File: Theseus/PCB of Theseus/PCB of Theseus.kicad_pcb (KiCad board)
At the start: 4 copper layers, 70 x 40 mm, 85 parts, among them J1 Conn_01x06_Socket, J2 Conn_01x06_Socket, J3 G125-MH104M4-04AD000P, J5 CN4 STDC14 (Programmer), J6 Micro SD Holder 0472192001, J7 4DB-P108-02, J8 Conn_01x12_Socket, Q1 DMG1012UW-7, Q2 DMG1012UW-7, U1 TPS565201DDC, U13 MAX6675, U2 MCP2562, U5 MX25L25645G, U6 STM32H750VBTx, Y1 ASE-4.000MHz-L-C-T

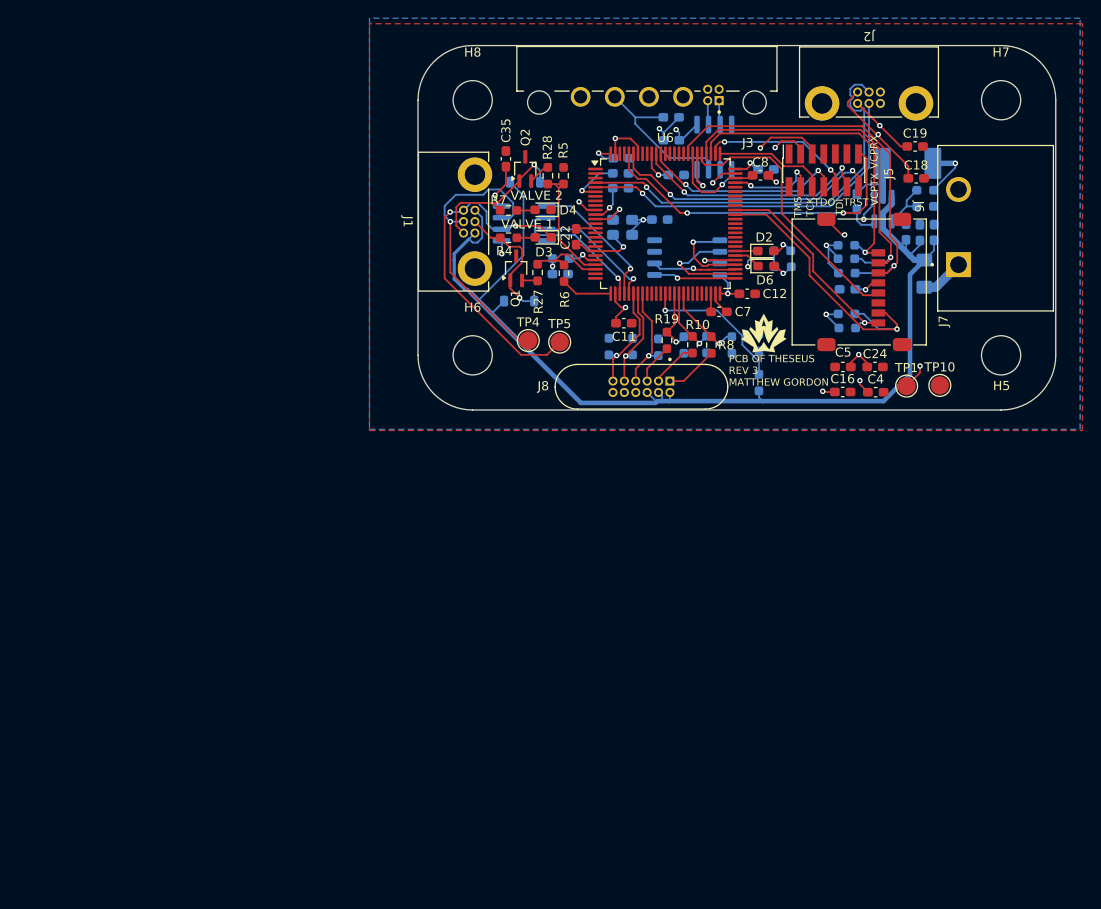
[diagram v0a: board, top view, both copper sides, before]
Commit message: layout and routing + minor schematic changes
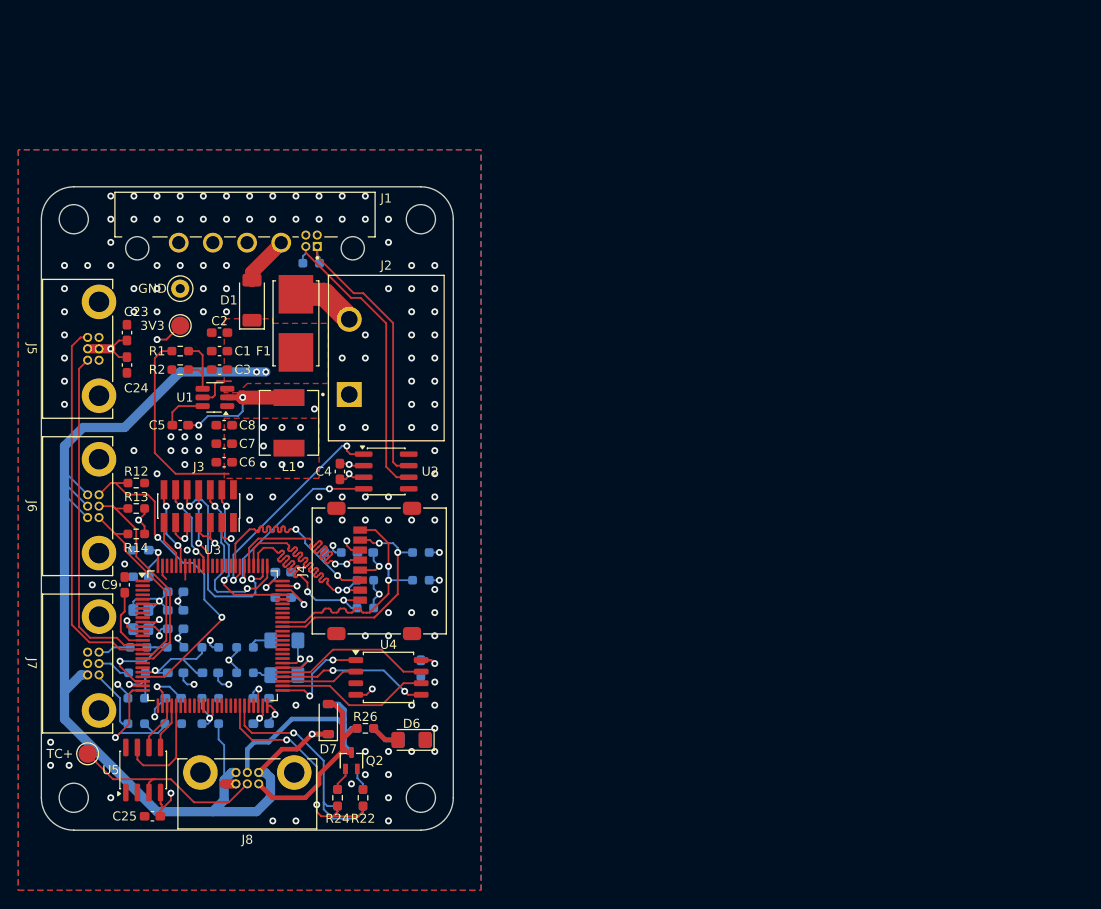
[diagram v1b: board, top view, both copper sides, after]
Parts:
- removed C32: 10u, Capacitor_SMD:C_0603_1608Metric_Pad1.08x0.95mm_HandSolder
- removed C35: 0.1u, Capacitor_SMD:C_0603_1608Metric_Pad1.08x0.95mm_HandSolder
- removed C40: 0.01uF, Capacitor_SMD:C_0603_1608Metric_Pad1.08x0.95mm_HandSolder
- removed the G*** at (152.9, 111.5)
- removed H5, H6, H7, H8: MountingHole, MountingHole:MountingHole_4.3mm_M4
- removed R28: 1k, Resistor_SMD:R_0603_1608Metric_Pad0.98x0.95mm_HandSolder
- removed R44, R45: 169R, Resistor_SMD:R_0603_1608Metric_Pad0.98x0.95mm_HandSolder
- removed R46: 300K, Resistor_SMD:R_0603_1608Metric_Pad0.98x0.95mm_HandSolder
- removed R47: 100K, Resistor_SMD:R_0603_1608Metric_Pad0.98x0.95mm_HandSolder
- removed TP1, TP10: TestPoint, TestPoint:TestPoint_Pad_D2.0mm
- removed TP4: TC1+, TestPoint:TestPoint_Pad_D2.0mm
- removed TP5: TC1-, TestPoint:TestPoint_Pad_D2.0mm
- removed U13: MAX6675, Package_SO:SOIC-8_3.9x4.9mm_P1.27mm
- removed U6: STM32H750VBTx, Package_QFP:LQFP-100_14x14mm_P0.5mm
- added 3V3: TestPoint, TestPoint:TestPoint_Pad_D2.0mm, F.Cu at (88.9, 110.7)
- added C20: 0.01uF, Capacitor_SMD:C_0603_1608Metric_Pad1.08x0.95mm_HandSolder, B.Cu at (88.4, 142.0)
- added C21: 4.7u, Capacitor_SMD:C_0603_1608Metric_Pad1.08x0.95mm_HandSolder, B.Cu at (84.6, 135.4)
- added C23: 0.1u, Capacitor_SMD:C_0603_1608Metric_Pad1.08x0.95mm_HandSolder, F.Cu at (83.1, 111.5)
- added D7: CDBW140-G, Diode_SMD:D_SOD-123, F.Cu at (105.2, 153.9)
- added G***: LOGO, Team_Logo:Logo_SilkScreen_10mm, B.Cu at (100.1, 110.2)
- added GND: TestPoint, TestPoint:TestPoint_Keystone_5000-5004_Miniature, F.Cu at (88.9, 106.7)
- added H1: MountingHole, MountingHole:MountingHole_3.2mm_M3_ISO14580, F.Cu at (77.2, 99.1)
- added H2: MountingHole, MountingHole:MountingHole_3.2mm_M3_ISO14580, F.Cu at (77.2, 162.6)
- added H3: MountingHole, MountingHole:MountingHole_3.2mm_M3_ISO14580, F.Cu at (115.3, 162.6)
- added H4: MountingHole, MountingHole:MountingHole_3.2mm_M3_ISO14580, F.Cu at (115.3, 99.1)
- added J4: Micro SD Holder 0472192001, Connector_Card:microSD_HC_Molex_47219-2001, F.Cu at (110.7, 137.7)
- added R21: 150k, Resistor_SMD:R_0603_1608Metric_Pad0.98x0.95mm_HandSolder, B.Cu at (106.2, 162.6)
- added R22: 150k, Resistor_SMD:R_0603_1608Metric_Pad0.98x0.95mm_HandSolder, F.Cu at (109.0, 162.6)
- added R23: 100R, Resistor_SMD:R_0603_1608Metric_Pad0.98x0.95mm_HandSolder, B.Cu at (109.0, 162.6)
- added R24: 100R, Resistor_SMD:R_0603_1608Metric_Pad0.98x0.95mm_HandSolder, F.Cu at (106.2, 162.6)
- added R25: 649R, Resistor_SMD:R_0603_1608Metric_Pad0.98x0.95mm_HandSolder, B.Cu at (109.2, 154.9)
- added R26: 649R, Resistor_SMD:R_0603_1608Metric_Pad0.98x0.95mm_HandSolder, F.Cu at (109.2, 154.9)
- added TC+: TC1+, TestPoint:TestPoint_Pad_D2.0mm, F.Cu at (78.7, 157.7)
- added U3: STM32H750VBTx, Package_QFP:LQFP-100_14x14mm_P0.5mm, F.Cu at (92.5, 144.8)
- added U4: MX25L25645G, Package_SO:SOIC-8_5.3x5.3mm_P1.27mm, F.Cu at (111.8, 149.4)
- C1, C25, C3, C9, U1: moved to F.Cu
- C10: value 100n -> 2.2u
- C11: value 100n -> 2.2u; moved to B.Cu
- C12, R19: moved to B.Cu
- C14: value 100n -> 1n
- C16: value 4.7u -> 100n; moved to B.Cu
- C17: value 1n -> 100n
- C18, C19: value 0.1u -> 100n; moved to B.Cu
- C2: value 100n -> 10u; moved to F.Cu
- C22: value 100n -> 10u; moved to B.Cu
- C24, C4: value 22u -> 0.1u
- C26: value 10u -> 100n
- C5: value 22u -> 100n
- C6: value 0.1u -> 22u; moved to F.Cu
- C7, C8: value 2.2u -> 22u
- D1: value CDBW140-G -> PMEG3030EP; footprint Diode_SMD:D_SOD-123 -> Diode_SMD:D_SOD-128; moved to F.Cu
- D2, D4: footprint Diode_SMD:D_0603_1608Metric_Pad1.05x0.95mm_HandSolder -> LED_SMD:LED_1206_3216Metric_Pad1.42x1.75mm_HandSolder; moved to B.Cu
- D3: value GREEN -> BLUE; footprint Diode_SMD:D_0603_1608Metric_Pad1.05x0.95mm_HandSolder -> LED_SMD:LED_1206_3216Metric_Pad1.42x1.75mm_HandSolder; moved to B.Cu
- D6: value BLUE -> GREEN; footprint Diode_SMD:D_0603_1608Metric_Pad1.05x0.95mm_HandSolder -> LED_SMD:LED_1206_3216Metric_Pad1.42x1.75mm_HandSolder
- F1: value 3.5A 0685T3500-01 -> 0154005.DRL; footprint Fuse:Fuse_1206_3216Metric_Pad1.42x1.75mm_HandSolder -> Fydp_footprints:FUSE_0154005.DR; moved to F.Cu
- J1: value Conn_01x06_Socket -> G125-MH104M4-04AD000P; footprint canhw_footprints:connector_Harwin_G125–MG10605M4P -> canhw_footprints:connector_Harwin_G125-MH104M4-04AD000P
- J2: value Conn_01x06_Socket -> 4DB-P108-02; footprint canhw_footprints:connector_Harwin_G125–MG10605M4P -> canhw_footprints:4DB-P108-02
- J3: value G125-MH104M4-04AD000P -> CN4 STDC14 (Programmer); footprint canhw_footprints:connector_Harwin_G125-MH104M4-04AD000P -> Connector_PinSocket_1.27mm:PinSocket_2x07_P1.27mm_Vertical_SMD
- J5: value CN4 STDC14 (Programmer) -> Conn_01x06_Socket; footprint Connector_PinSocket_1.27mm:PinSocket_2x07_P1.27mm_Vertical_SMD -> canhw_footprints:connector_Harwin_G125–MG10605M4P
- J6: value Micro SD Holder 0472192001 -> Conn_01x06_Socket; footprint Connector_Card:microSD_HC_Molex_47219-2001 -> canhw_footprints:connector_Harwin_G125–MG10605M4P
- J7: value 4DB-P108-02 -> Conn_01x06_Socket; footprint canhw_footprints:4DB-P108-02 -> canhw_footprints:connector_Harwin_G125–MG10605M4P
- J8: value Conn_01x12_Socket -> Conn_01x06_Socket; footprint canhw_footprints:connector_Harwin_G125-MV11205M1P -> canhw_footprints:connector_Harwin_G125–MG10605M4P
- L1: value 2.2u -> SPM6530T-2R2M; footprint Fydp_footprints:SPM6530T-2R2M -> Fydp_footprints:IND_SPM6530T-2R2M; moved to F.Cu
- Q1: footprint Package_TO_SOT_SMD:SOT-323_SC-70_Handsoldering -> Fydp_footprints:SOT_12UW-7_DIO; moved to B.Cu
- Q2: footprint Package_TO_SOT_SMD:SOT-323_SC-70_Handsoldering -> Fydp_footprints:SOT_12UW-7_DIO
- R1: value 150R ±0.1% -> 33.2k; moved to F.Cu
- R10, R8: value 82K -> 51k; moved to B.Cu
- R11: value 33.2k -> 51k
- R12: value 10k -> 150R ±0.1%; moved to F.Cu
- R13, R14: value 51k -> 150R ±0.1%; moved to F.Cu
- R15, R17: value 51k -> 82K
- R16: value 51k -> 130K
- R2: value 150R ±0.1% -> 10k; moved to F.Cu
- R27: value 1k -> 120R; moved to B.Cu
- R3: value 150R ±0.1% -> 300K
- R4: value 649R -> 100K; moved to B.Cu
- R5, R6: value 150k -> 169R; moved to B.Cu
- R7: value 649R -> 51k; moved to B.Cu
- R9: value 130K -> 51k
- U2: value MCP2562 -> TCAN334; moved to F.Cu
- U5: value MX25L25645G -> MAX6675; footprint Package_SO:SOIC-8_5.3x5.3mm_P1.27mm -> Package_SO:SOIC-8_3.9x4.9mm_P1.27mm; moved to F.Cu
- moved J7 104.0 mm to (80.0, 147.8), turned to -90 degrees
- moved C19 97.2 mm to (84.6, 138.3), turned to 180 degrees
- moved C25 93.5 mm to (85.9, 164.6)
- moved R12 91.8 mm to (84.1, 128.0)
- moved R15 87.9 mm to (84.3, 146.1)
- moved J6 87.0 mm to (80.0, 130.6)
- moved R17 86.7 mm to (84.2, 148.8)
- moved R14 83.6 mm to (84.1, 133.6)
- moved R13 83.1 mm to (84.1, 130.8)
- moved R16 82.2 mm to (88.4, 146.1)
- moved C24 82.1 mm to (83.1, 115.1), turned to -90 degrees
- moved C15 82.1 mm to (88.4, 144.0)
- moved U5 82.0 mm to (84.8, 159.5), turned to 90 degrees
- moved J5 81.9 mm to (80.0, 113.3), turned to -90 degrees
- moved C18 81.8 mm to (100.2, 137.8)
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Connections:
- C10 pad 1: +3.3V -> Net-(C10-Pad1)
- C11 pad 1: +3.3V -> Net-(C11-Pad1)
- C13 pad 1: +3.3V -> /MCU/VDDA
- C14 pad 1: +3.3V -> /MCU/VDDA
- C22 pad 1: Net-(U6-NRST) -> +3.3V
- C3 pad 1: Net-(U1-SW) -> +BATT
- C3 pad 2: Net-(U1-VBST) -> GND
- C5 pad 1: +3.3V -> Net-(U1-SW)
- C5 pad 2: GND -> Net-(U1-VBST)
- C6 pad 1: +5V -> +3.3V
- C7 pad 1: Net-(C7-Pad1) -> +3.3V
- C8 pad 1: Net-(C8-Pad1) -> +3.3V
- C9 pad 1: +3.3V -> Net-(U3-NRST)
- D2 pad 1: /MCU/LED_BLUE -> /MCU/LED_W
- D3 pad 1: GND -> /MCU/LED_B
- D6 pad 1: /MCU/LED_RED -> GND
- F1 pad 2: Net-(J7-Pin_1) -> Net-(J2-Pin_2)
- FB1 pad 2: Net-(U6-VDDA) -> /MCU/VDDA
- J1 pad 1: +BATT -> /CANH
- J1 pad 2: Net-(D1-A) -> /CANL
- J1 pad 3: +BATT -> unconnected-(J1-NC-Pad3)
- J1 pad 4: Net-(D5-A) -> unconnected-(J1-NC-Pad4)
- J2 pad 1: +3.3V -> GND
- J2 pad 2: /MCU/HALL_1 -> Net-(J2-Pin_2)
- J3 pad 1: /CANH -> unconnected-(J3-Pin_1-Pad1)
- J3 pad 2: /CANL -> unconnected-(J3-Pin_2-Pad2)
- J3 pad 3: unconnected-(J3-NC-Pad3) -> +3.3V
- J3 pad 4: unconnected-(J3-NC-Pad4) -> /MCU/TMS
- J5 pad 1: unconnected-(J5-Pin_1-Pad1) -> GND
- J5 pad 2: unconnected-(J5-Pin_2-Pad2) -> +3.3V
- J5 pad 3: +3.3V -> GND
- J5 pad 4: /MCU/TMS -> /MCU/HALL_1
- J5 pad 5: GND -> +3.3V
- J5 pad 6: /MCU/TCK -> /MCU/HALL_2
- J6 pad 1: /MCU/SD_D2 -> /Valves and Sensors/PT1_OUT
- J6 pad 2: /MCU/SD_D3 -> /Valves and Sensors/PT2_OUT
- J6 pad 3: /MCU/SD_CMD -> /Valves and Sensors/PT3_OUT
- J6 pad 4: +3.3V -> +BATT
- J6 pad 5: /MCU/SD_CLK -> +BATT
- J6 pad 6: GND -> +BATT
- J7 pad 1: Net-(J7-Pin_1) -> /Valves and Sensors/PT4_OUT
- J7 pad 2: GND -> /Valves and Sensors/PT5_OUT
- J8 pad 1: /Valves and Sensors/PT4_OUT -> +BATT
- J8 pad 2: /Valves and Sensors/PT5_OUT -> Net-(D5-A)
- J8 pad 3: /Valves and Sensors/PT6_OUT -> +BATT
- J8 pad 4: /Valves and Sensors/PT1_OUT -> Net-(D7-A)
- J8 pad 5: /Valves and Sensors/PT2_OUT -> /Valves and Sensors/TC1+
- J8 pad 6: /Valves and Sensors/PT3_OUT -> GND
- Q1 pad 1: Net-(D1-A) -> Net-(Q1-G)
- Q1 pad 2: Net-(Q1-G) -> GND
- Q1 pad 3: GND -> Net-(D5-A)
- Q2 pad 1: Net-(D5-A) -> Net-(Q2-G)
- Q2 pad 2: Net-(Q2-G) -> GND
- Q2 pad 3: GND -> Net-(D7-A)
- R1 pad 1: /Valves and Sensors/PT1_OUT -> +3.3V
- R1 pad 2: GND -> Net-(U1-VFB)
- R10 pad 1: /Valves and Sensors/PT5_OUT -> +3.3V
- R10 pad 2: /MCU/PT5 -> /MCU/SD_D0
- R11 pad 2: Net-(U1-VFB) -> /MCU/SD_D1
- R12 pad 1: Net-(U1-VFB) -> /Valves and Sensors/PT3_OUT
- R13 pad 1: +3.3V -> /Valves and Sensors/PT2_OUT
- R13 pad 2: /MCU/SD_D2 -> GND
- R14 pad 1: +3.3V -> /Valves and Sensors/PT1_OUT
- R14 pad 2: /MCU/SD_D3 -> GND
- R15 pad 1: +3.3V -> /Valves and Sensors/PT6_OUT
- R15 pad 2: /MCU/SD_CMD -> /MCU/PT6
- R16 pad 1: +3.3V -> /MCU/PT6
- R16 pad 2: /MCU/SD_D0 -> GND
- R17 pad 1: +3.3V -> /Valves and Sensors/PT5_OUT
- R17 pad 2: /MCU/SD_D1 -> /MCU/PT5
- R19 pad 1: /Valves and Sensors/PT6_OUT -> /Valves and Sensors/PT4_OUT
- R19 pad 2: /MCU/PT6 -> /MCU/PT4
- R2 pad 1: /Valves and Sensors/PT2_OUT -> Net-(U1-VFB)
- R20 pad 1: /MCU/PT6 -> /MCU/PT4
- R27 pad 1: Net-(Q1-G) -> /CANH
- R27 pad 2: /MCU/VALVE_1 -> /CANL
- R3 pad 1: /Valves and Sensors/PT3_OUT -> +BATT
- R3 pad 2: GND -> /MCU/V_BATT
- R4 pad 1: Net-(D1-A) -> /MCU/V_BATT
- R4 pad 2: Net-(D3-A) -> GND
- R5 pad 1: /MCU/VALVE_2 -> +3.3V
- R5 pad 2: GND -> Net-(D2-A)
- R6 pad 1: /MCU/VALVE_1 -> +3.3V
- R6 pad 2: GND -> Net-(D3-A)
- R7 pad 1: Net-(D5-A) -> +3.3V
- R7 pad 2: Net-(D4-A) -> /MCU/SD_D2
- R8 pad 1: /Valves and Sensors/PT4_OUT -> +3.3V
- R8 pad 2: /MCU/PT4 -> /MCU/SD_D3
- R9 pad 1: /MCU/PT4 -> +3.3V
- R9 pad 2: GND -> /MCU/SD_CMD
- U2 pad 3: +5V -> +3.3V
- U2 pad 5: +3.3V -> GND
- U5 pad 1: /MCU/SPI_NSS -> GND
- U5 pad 2: /MCU/SPI_MISO -> GND
- U5 pad 3: unconnected-(U5-WP#/SIO2-Pad3) -> /Valves and Sensors/TC1+
- U5 pad 4: GND -> +3.3V
- U5 pad 5: /MCU/SPI_MOSI -> /MCU/TC1_SCK
- U5 pad 6: /MCU/SPI_SCK -> /MCU/~{TC1_CS}
- U5 pad 7: /MCU/MEM_~{RESET} -> /MCU/TC1_MISO
- U5 pad 8: +3.3V -> unconnected-(U5-N.C.-Pad8)
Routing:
- net GND: track 85.9 -> 47.1 mm, vias 12 -> 141
- net /MCU/VCP_RX: track 36.8 -> 5.30 mm, vias 2 -> 0
- net /CANL: track 2.66 -> 33.4 mm
- net /CANH: track 2.67 -> 31.6 mm
- net /Valves and Sensors/PT3_OUT: track 12.1 -> 36.8 mm, vias 1 -> 2
- net Net-(D7-A): track 0.00 -> 22.1 mm
- net /MCU/VCP_TX: track 30.9 -> 9.11 mm
- net /MCU/SD_CMD: track 44.6 -> 24.7 mm, vias 1 -> 2
- net +5V: track 17.7 -> 0.00 mm
- net /MCU/~{FLASH_RESET}: track 0.00 -> 17.2 mm
- net /MCU/FLASH_SCK: track 0.00 -> 17.1 mm
- net /MCU/TRST: track 26.6 -> 9.74 mm
- net /MCU/FLASH_MOSI: track 0.00 -> 16.6 mm, vias 0 -> 2
- net /MCU/VALVE_1: track 8.68 -> 25.2 mm, vias 0 -> 1
- net /MCU/TC1_NSS: track 15.8 -> 0.00 mm, vias 1 -> 0
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- added copper zone on F.Cu, net +3.3V
- added copper zone on F.Cu, net +BATT
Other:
- board size 70 x 40 mm -> 45.2 x 70.6 mm
- board text added: "PCB of Theseus 03/2026 Matthew Gordon, Ash Lang"
- board text removed: "PCB OF THESEUS REV 3 MATTHEW GORDON"
- board text removed: "TCK"
- board text removed: "TDI"
- board text removed: "TDO"
- board text removed: "TMS"
- board text removed: "TRST"
- board text removed: "VALVE 1"
- board text removed: "VALVE 2"
- board text removed: "VCPRX"
- board text removed: "VCPTX"

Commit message: minor fixes, generate prod files + reference files
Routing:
- net GND: track 47.1 -> 48.3 mm, vias 141 -> 144
- net /MCU/PT4: track 14.8 -> 13.8 mm
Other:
- board text added: "0-5V"
- board text added: "4-20mA"
- board text added: "Hall"
- board text added: "TC + Valves"
